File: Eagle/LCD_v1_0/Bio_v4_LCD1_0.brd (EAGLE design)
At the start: 100 x 84.6 mm, 117 parts, among them CON1 JACK_DC_BARREL, IC1 MCP1703DB, IC3 SN74LVC2G14, J1 RJ12RIGHTANGLE-I2C, J2 RJ12RIGHTANGLE-I2C, J7 22--02, Q1 BSP75, Q2 BSP75, Q3 BSP75, Q4 BSP75, Q5 BSP75, Q6 BSP75, U1 HX711, U100 RN2483, X2 8MHz, X3 FH12-08S-1SH, X4 MINI-USB

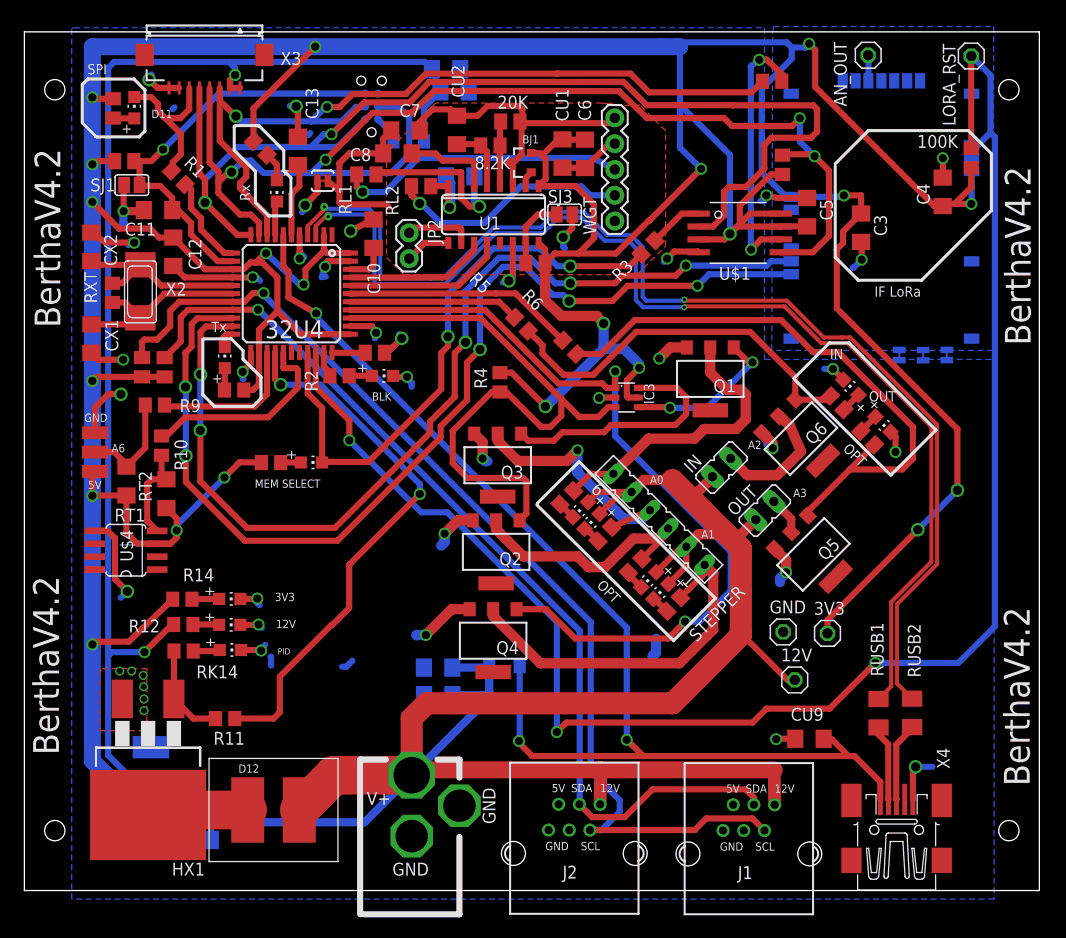
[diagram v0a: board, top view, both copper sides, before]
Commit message: LCD v1_0, compatible with v4_2 of the main board, 5V generated on board w NCP1117
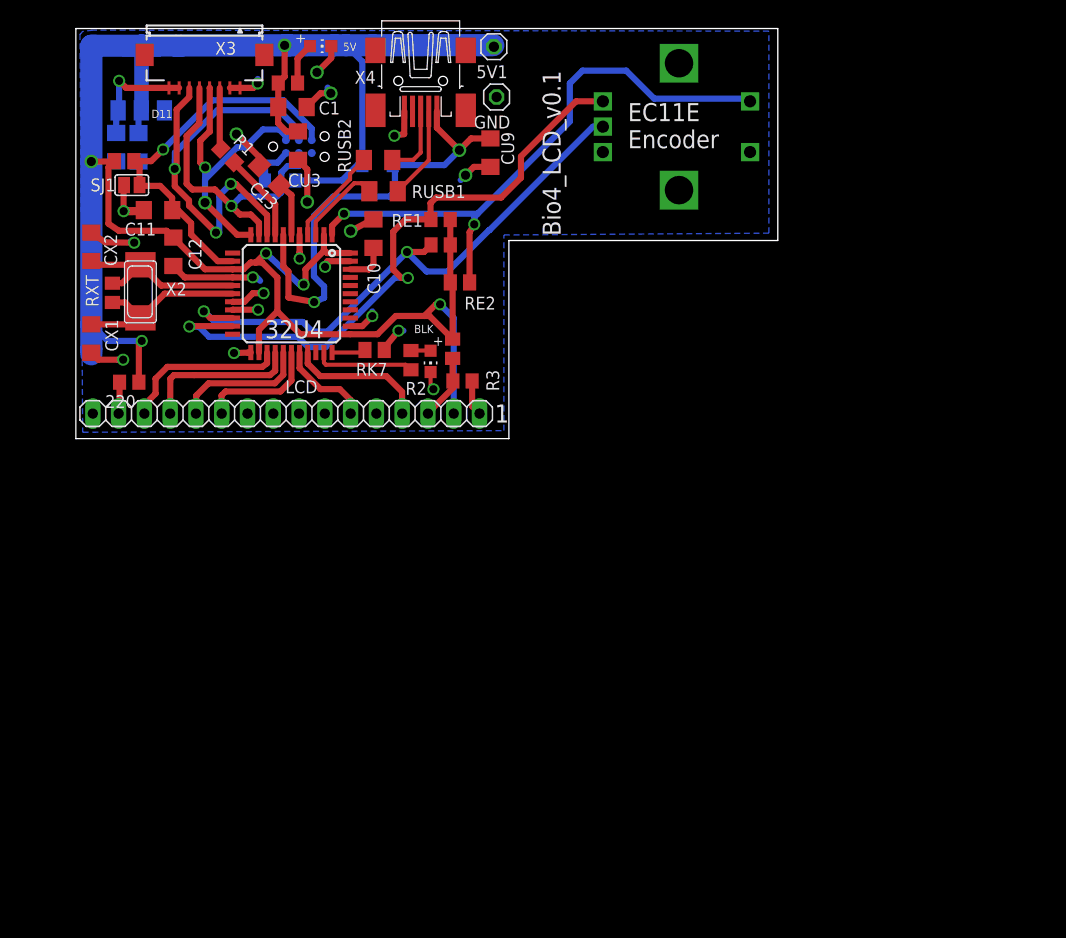
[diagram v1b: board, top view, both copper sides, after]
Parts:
- removed 100K: 100k, rcl:R0805
- removed 12V, 3V3, AN_OUT, LORA_RST: (no value), Headerlibrary:1X01
- removed 20K: 20k, resistor:M0805
- removed 8.2K: 8.2k, resistor:M0805
- removed BJ1: MMBT4403, SparkFun-DiscreteSemi:SOT23-3
- removed C2, C3, C4, C5, C6, C7, C8, C9: 100nF, rcl:C1206
- removed CON1: JACK_DC_BARREL, lpatiny:DC_BARREL
- removed CU1, CU2, CU4, CU7, CU8: 10uF, rcl:C1206
- removed HX1: IRF3704S, transistor-power:D2PACK
- removed IC1: MCP1703DB, linear:SOT223
- removed IC3: SN74LVC2G14, lpatiny:SOT23-6
- removed IN, OUT: (no value), jumper:JP1
- removed J1, J2: RJ12RIGHTANGLE-I2C, lpatiny:RJ12-RIGHTANGLE-I2C
- removed J7: 22--02, lpatiny:2-PIN-5.08S
- removed JP2: (no value), SparkFun-Connectors:1X02
- removed LDIN, LDM1, LDM2, LDM3, LDM4, LDMEM, LDOUT, LDPID, LDPW12, LDPW3, LDSLAVE, RXLD, TXLD: RED, adafruit:CHIP-LED0805
- removed Q1, Q2, Q3, Q4, Q5, Q6: BSP75, infineon:PG-SOT-223
- removed R10, R11, R4, R5, R6, R9: 1K, rcl:R0805
- removed R12: 1k, rcl:R0805
- removed R14: 1k, resistor:R0805
- removed RK10, RK11, RK8, RK9: 10K, rcl:R0805
- removed RK12, RK13, RK14, RK15, RK16, RK18, RK19, RK3, RK4: 10k, rcl:R0805
- removed RK5: 10k, resistor:M0805
- removed RL1, RL2: 100, resistor:M0805
- removed RT1, RT2: 4.7k, resistor:R1206
- removed SJ2, SJ4, SJ5, SJ6: (no value), SparkFun-Passives:PAD-JUMPER-2-NC_BY_TRACE_YES_SILK
- removed SJ3: (no value), jumper:SJ
- removed STEPPER: (no value), con-lsta:FE06
- removed U$4: DS18B20, lpatiny:SO8
- removed U$8: DS18B20_SMALLPADS, lpatiny:SMALLPADS_X3
- removed U1: HX711, Testing:SO16
- removed U100: RN2483, Octanis1:RN2483
- removed WGT: (no value), SparkFun-Connectors:1X05
- added 220: 220, rcl:R0805
- added 5V1: (no value), Headerlibrary:1X01
- added CU5, CU6: 10uF, rcl:C1206
- added LCD: (no value), lpatiny:1X16
- added LDO: NCP1117LPST50T3G, lpatiny:SOT223
- added LDPW5: RED, adafruit:CHIP-LED0805
- added R13: 1k, resistor:R0805
- added RE1, RE2: 5k, rcl:R0805
- 32U4: value ATMEGA32U4 -> 32U4
- R2: value 10k -> 1k
- RK1: value 10K -> 10k; device resistor:M0805 -> rcl:R0805
- RK2: value 10K -> 10k
- U$1: value SST25VF064C -> EC11E; device BertaLib:SOIC_8-LEAD -> lpatiny:EC11E
- X2: value 8MHz -> 16MHz
- moved X4 87.4 mm to (34.0, 76.9), turned to 270 degrees
- moved RUSB2 75.7 mm to (29.9, 69.1), turned to 0 degrees
- moved RUSB1 70.9 mm to (30.4, 66.0), turned to 0 degrees
- moved CU9 65.7 mm to (40.9, 69.8), turned to 90 degrees
- moved GND 59.8 mm to (41.5, 75.3), turned to 180 degrees
- moved D4 50.9 mm to (29.8, 68.6)
- moved RK2 32.4 mm to (37.9, 57.0), turned to 180 degrees
- moved RK1 28.4 mm to (37.2, 50.5), turned to 270 degrees
- moved R3 22.5 mm to (38.2, 47.3), turned to 0 degrees
- moved CU3 16.3 mm to (22.0, 70.5), flipped to the top, turned to 270 degrees
- moved U$1 16.2 mm to (52.0, 72.4)
- moved C1 15.6 mm to (21.4, 74.3), flipped to the top, turned to 0 degrees
- moved D2 13.2 mm to (20.2, 67.1)
- moved CON_ISP 9.81 mm to (19.5, 70.4), turned to 180 degrees
- moved R2 7.20 mm to (33.1, 49.4), turned to 90 degrees
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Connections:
- removed net 3.3V: 100K.1, 32U4.14, 32U4.2, 32U4.24, 32U4.34, 32U4.44, 3V3.1, BJ1.2, C12.2, C3.1, C4.1, C5.2, C6.1, CU1.1, CU8.1, IC1.3, IC3.5, R14.1, R4.2, RK1.1, RK15.1, RK16.1, RK18.1, RK19.1, RK2.1, RK4.2, RK5.2, RK6.2, RT1.1, RT2.1, U$1.RST/HOLD, U$1.VDD, U$1.WP, U$4.3, U$8.PIN3, U1.1, U1.16, U100.P$12, U100.P$34
- removed net 5: J1.+5V, J2.+5V
- removed net A+: RL2.2, WGT.2
- removed net A-: RL1.2, WGT.3
- removed net ANGND: C3.2, C4.2, SJ4.2, SJ5.2, SJ6.2, U100.P$1, U100.P$11, U100.P$20, U100.P$21, U100.P$22, U100.P$24, U100.P$26, U100.P$27, U100.P$28, U100.P$33, U100.P$41, U100.P$47, U100.P$8
- removed net ANT868: AN_OUT.1, U100.P$23
- removed net B+: JP2.1, U1.10
- removed net B-: JP2.2, U1.9
- removed net CN3: C8.2, U1.6
- removed net LGND: 8.2K.1, C7.2, C8.1, CU2.2, SJ2.2, U1.5
- removed net N$10: R3.1, U$1.CE
- removed net N$13: OUT.2, Q5.2
- removed net N$14: Q4.2, RK8.1, STEPPER.1
- removed net N$15: Q2.2, RK9.1, STEPPER.3
- removed net N$16: Q3.2, RK10.1, STEPPER.4
- removed net N$17: IN.2, Q6.2
- removed net N$18: RK15.2, TXLD.A
- removed net N$19: Q1.2, RK11.1, STEPPER.6
- removed net N$20: C9.2, RL1.1, U1.7
- removed net N$21: R9.2, RT1.2, U$8.PIN2
- removed net N$22: LDSLAVE.A, RK18.2
- removed net N$23: RK3.2, U$1.SCK
- removed net N$24: RK16.2, RXLD.A
- removed net N$25: LDMEM.A, RK19.2
- removed net N$26: LDPID.A, RK14.1
- removed net N$27: LDIN.A, RK12.1
- removed net N$28: LDOUT.A, RK13.1
- removed net N$29: IC3.6, Q3.1
- removed net N$30: IC3.4, Q1.1
- removed net N$31: LDM4.C, RK8.2
- removed net N$32: LDM3.C, RK9.2
- removed net N$33: LDM2.C, RK10.2
- removed net N$34: LDPW3.A, R14.2
- removed net N$36: HX1.2, J7.2
- removed net N$37: LDM1.C, RK11.2
- removed net N$38: BJ1.1, U1.2
- removed net N$39: 20K.1, 8.2K.2, U1.4
- removed net N$41: RK5.1, SJ3.1, U1.15
- removed net N$43: C9.1, RL2.1, U1.8
- removed net N$5: 20K.2, BJ1.3, C7.1, CU2.1, U1.3, WGT.5
- removed net N$6: HX1.1, R11.2, RK14.2
- removed net N$7: LDPW12.A, R12.1
- removed net N$8: Q6.1, R5.2, RK12.2
- removed net N$9: R10.2, RT2.2, U$4.4
- new net +5V/1: 220.1, 32U4.14, 32U4.2, 32U4.24, 32U4.34, 32U4.44, 5V1.1, C1.1, C12.2, CU3.1, CU5.1, D2.C, D4.C, LCD.2, LDO.2, LDO.4, R13.1, RE1.1, RE2.1, RK1.1, RK2.2, RK6.2
- new net N$12: LDPW5.A, R13.2
- new net N$2: LCD.3, R3.1, RK1.2
- net +12V: now also CU6.1, LDO.3, X3.7, X3.8; no longer 12V.1, C1.1, C2.1, CON1.P$1, CU3.1, CU4.1, CU7.1, D2.C, D4.C, IC1.1, IN.1, J1.+12V, J2.+12V, J7.1, LDM1.A, LDM2.A, LDM3.A, LDM4.A, OUT.1, R12.2, STEPPER.2, STEPPER.5, X3.1, X3.2
- net A0: no longer IC3.3, Q2.1, R4.1
- net A1: no longer IC3.1, Q4.1
- net A2: no longer R5.1
- net A3: no longer R6.1
- net A4: no longer U1.12
- net A5: no longer U1.11
- net A6: now also LCD.14; no longer R9.1
- net CS_32U4: now also X3.3; no longer LDSLAVE.C, X3.6
- net D10*: now also LCD.4; no longer LDMEM.C, R3.2
- net D11*: no longer R1.2
- net D12*: now also LCD.13; no longer R11.1
- net D5*: no longer 100K.2, LORA_RST.1, U100.P$32
- net D6*: now also LCD.12; no longer R10.1
- net D7*: now also RK2.1, U$1.D
- net D8*: now also LCD.11
- net D9*: now also LCD.6
- net GND: now also CU5.2, CU6.2, LCD.1, LCD.16, LCD.5, LDO.1, LDPW5.C, R3.2, U$1.C, U$1.E, X3.1, X3.2; no longer C2.2, C5.1, C6.2, CON1.P$2, CU1.2, CU4.2, CU7.2, CU8.2, HX1.3, IC1.2, IC3.2, J1.GND1, J1.GND2, J2.GND1, J2.GND2, LDIN.C, LDOUT.C, LDPID.C, LDPW12.C, LDPW3.C, Q1.3, Q2.3, Q3.3, Q4.3, Q5.3, Q6.3, SJ2.1, SJ3.2, SJ4.1, SJ5.1, SJ6.1, U$1.VSS, U$4.5, U$8.PIN1, U1.14, WGT.1, WGT.4, X3.7, X3.8
- net MISO: now also X3.4; no longer U$1.SO, X3.5
- net MOSI: now also X3.5; no longer RK4.1, U$1.SI, X3.4
- net N$11: now also 220.2, LCD.15; no longer Q5.1, R6.2, RK13.2
- net RX: now also RE2.2, U$1.B; no longer U100.P$6
- net RXLED: now also R1.2; no longer RXLD.C
- net SCK: now also X3.6; no longer RK3.1, X3.3
- net SCL: no longer J1.SCL, J2.SCL, RK2.2
- net SDA: no longer J1.SDA, J2.SDA, RK1.2
- net TX: now also RE1.2, U$1.A; no longer U100.P$7
- net TXLED: no longer TXLD.C
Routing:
- net 3.3V: track 516.1 -> 0.00 mm, vias 21 -> 0
- net +12V: track 334.8 -> 11.5 mm, vias 2 -> 1
- net +5V/1: track 0.00 -> 217.8 mm, vias 0 -> 6
- net D5*: track 164.8 -> 0.00 mm, vias 3 -> 0
- net USB_P: track 114.0 -> 9.66 mm, vias 2 -> 0
- net USB_N: track 112.3 -> 8.47 mm, vias 2 -> 0
- net SCL: track 103.9 -> 3.58 mm
- net SDA: track 94.3 -> 2.56 mm
- net MOSI: track 119.9 -> 30.6 mm, vias 4 -> 1
- net MISO: track 112.0 -> 28.4 mm
- net A1: track 81.4 -> 0.00 mm, vias 2 -> 0
- net GND: track 148.1 -> 69.8 mm, vias 40 -> 18
- net VUSB: track 116.1 -> 45.8 mm, vias 3 -> 2
- net A0: track 61.7 -> 0.00 mm
- net D7*: track 0.00 -> 58.9 mm, vias 0 -> 2
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- removed copper zone on layer 16, net ANGND
- removed copper zone on layer 1, net GND
- removed copper zone on layer 1, net LGND
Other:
- board size 100 x 84.6 mm -> 69.2 x 40.4 mm
- board text added: "1"
- board text added: "Bio4_LCD_v0.1"
- board text added: "EC11E Encoder"
- board text added: "Screen v0.1"
- board text removed: "12V"
- board text removed: "3V3"
- board text removed: "A0"
- board text removed: "A1"
- board text removed: "A2"
- board text removed: "A3"
- board text removed: "A6"
- board text removed: "BerthaV4.2"
- board text removed: "D12"
- board text removed: "GND"
- board text removed: "IF LoRa"
- board text removed: "IN"
- board text removed: "LoRa RN2483"
- board text removed: "MEM SELECT"
- board text removed: "OPT"
- board text removed: "OUT"
- board text removed: "PID"
- board text removed: "Rx"
- board text removed: "SPI"
- board text removed: "Screen"
- board text removed: "Tx"

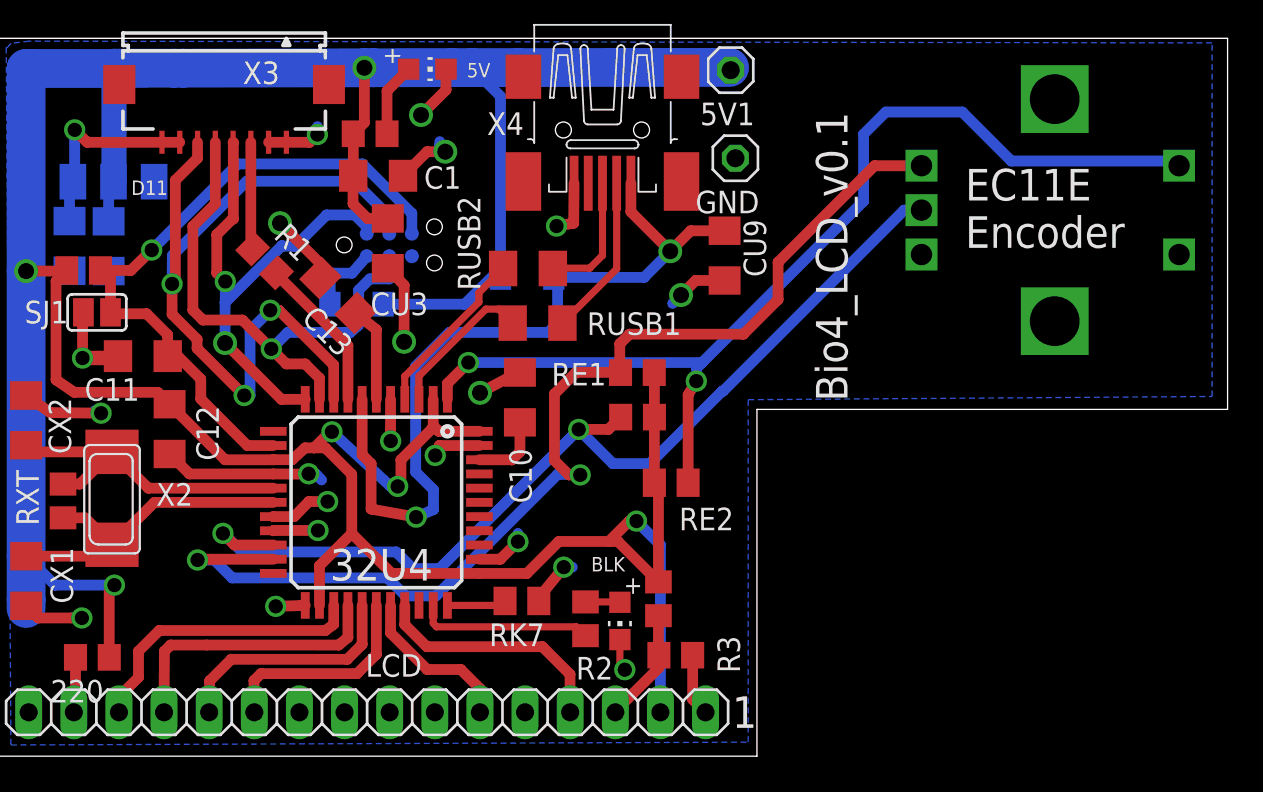
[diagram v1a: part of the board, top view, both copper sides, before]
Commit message: corrected DRC for microcuircuitos on LCD board (0.25mm clearance)
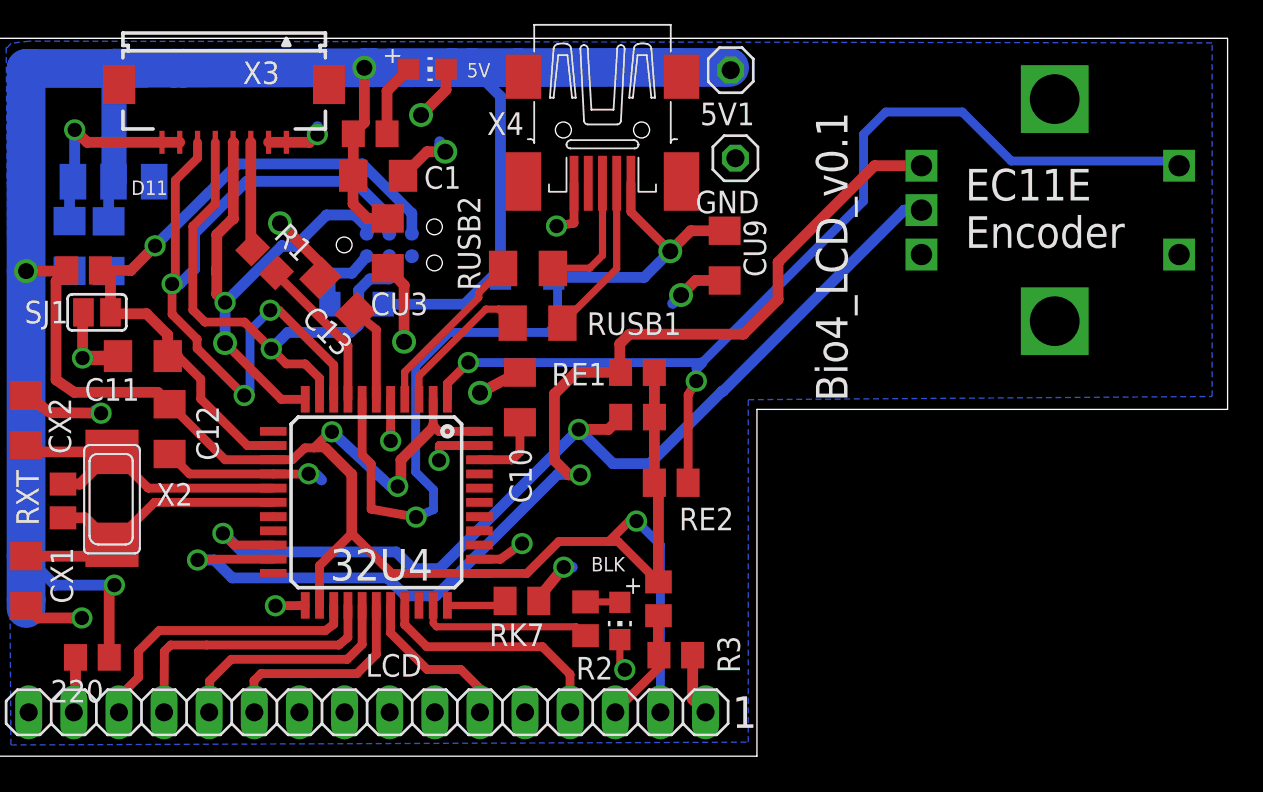
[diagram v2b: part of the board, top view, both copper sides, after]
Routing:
- net SCL: track 3.58 -> 0.01 mm, vias 1 -> 0
- net SDA: track 2.56 -> 0.00 mm, vias 1 -> 0
